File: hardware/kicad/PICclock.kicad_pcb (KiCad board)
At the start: 4 copper layers, 45 x 65 mm, 25 parts, among them J1 ICSP, J2 CLK_OUT, SW1 VAR/STEP, SW2 HS/[VAR/STEP], SW3 STEP, U1 PIC16F18344-P, U2 74HCT00, U3 EL7232CNZ, Y1 25MHz, Y2 CXO_DIP14

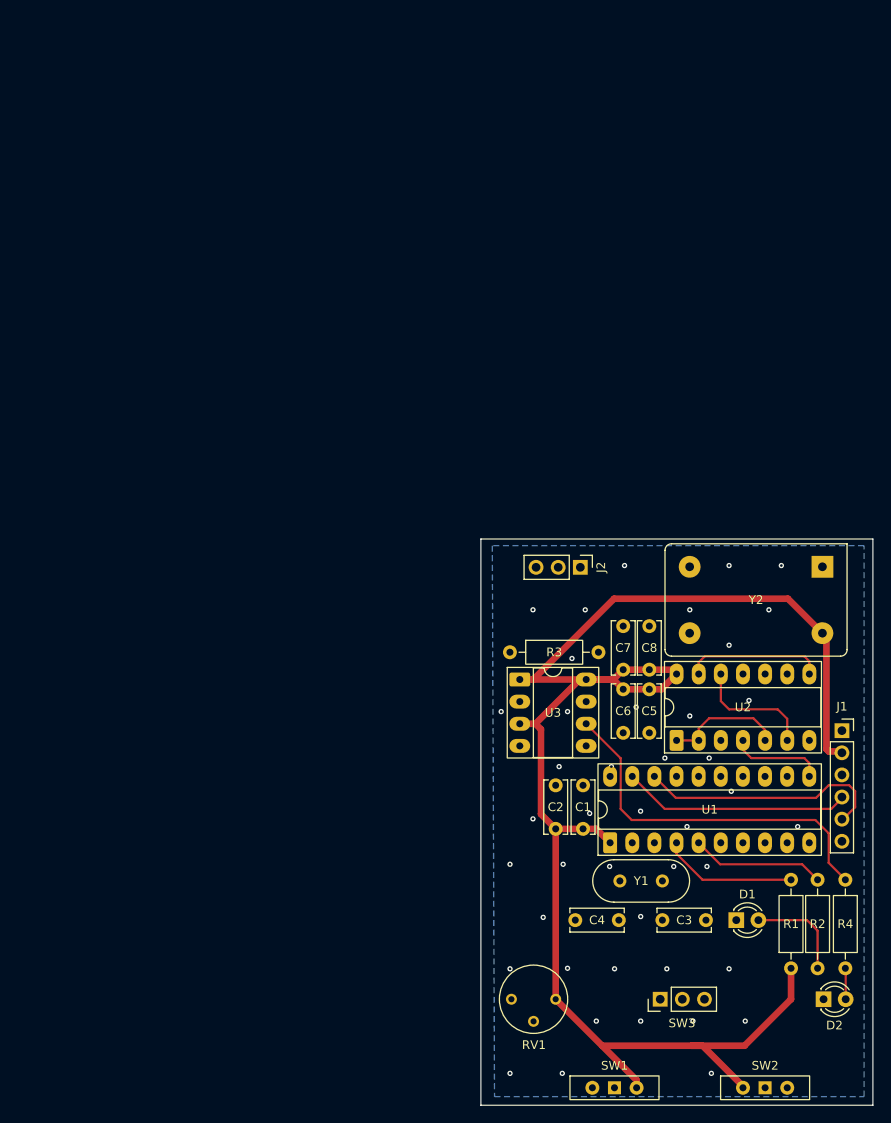
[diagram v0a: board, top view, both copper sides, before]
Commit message: add power input
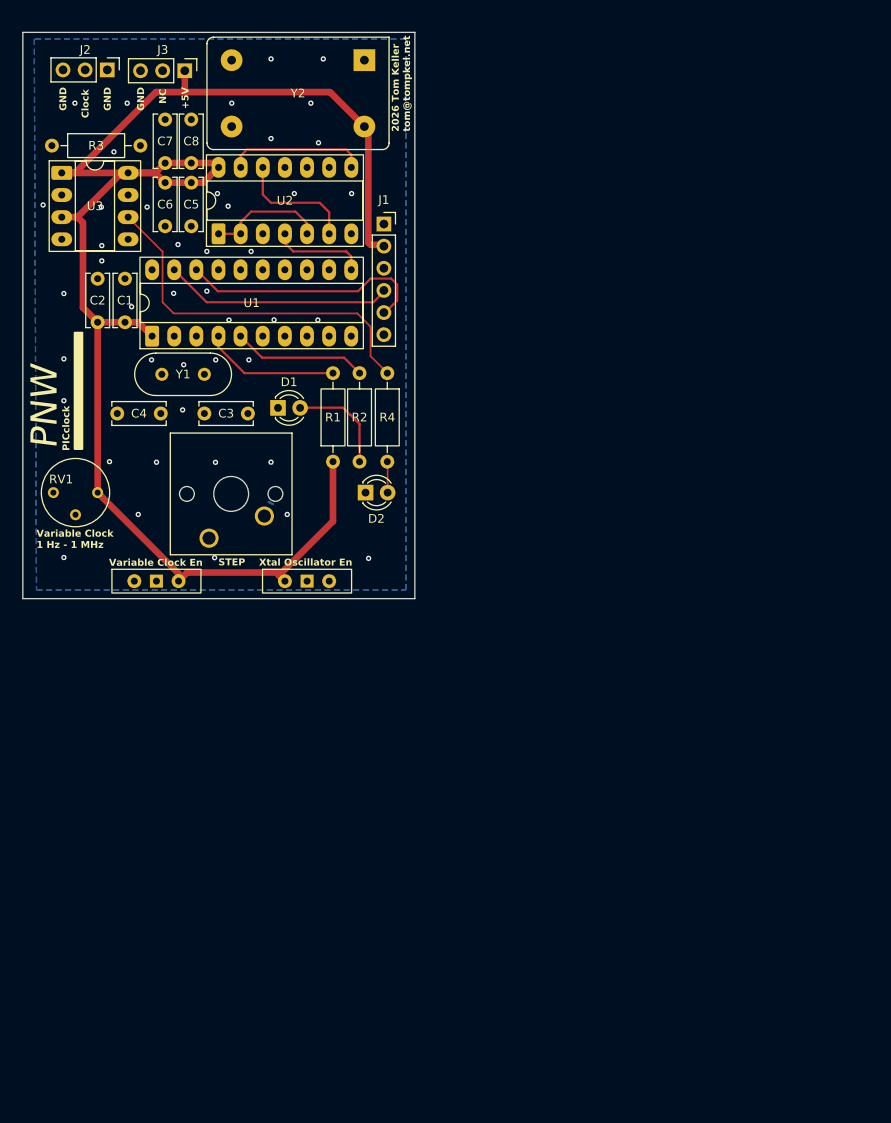
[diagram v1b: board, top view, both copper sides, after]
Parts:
- added J3: PWR_IN, Connector_PinHeader_2.54mm:PinHeader_1x03_P2.54mm_Vertical, F.Cu at (26.7, 9.75)
- SW3: footprint Connector_PinHeader_2.54mm:PinHeader_1x03_P2.54mm_Vertical -> Button_Switch_Keyboard:SW_Cherry_MX_1.00u_PCB
- moved D1 78.9 mm to (37.4, 48.5)
- moved J2 78.8 mm to (17.8, 9.65)
- moved SW1 78.4 mm to (23.4, 68.3)
- moved SW2 78.4 mm to (40.7, 68.3)
- moved C1 78.4 mm to (19.8, 33.6)
- moved C2 78.4 mm to (16.7, 38.6)
- moved C3 78.4 mm to (33.9, 49.1)
- moved C4 78.4 mm to (23.9, 49.1)
- moved C5 78.4 mm to (27.4, 27.6)
- moved C6 78.4 mm to (24.4, 22.6)
- moved C7 78.4 mm to (24.4, 15.3)
- moved C8 78.4 mm to (27.4, 20.3)
- moved D2 78.4 mm to (47.4, 58.2)
- moved J1 78.4 mm to (49.5, 27.3)
- moved R1 78.4 mm to (43.7, 54.6)
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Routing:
- net Net-(U1-RC4): track 20.8 -> 26.2 mm
- net Net-(J2-Pin_2): track 14.0 -> 10.3 mm
- net +5V: track 184.8 -> 181.7 mm
- net Net-(U1-RA4): track 11.5 -> 10.3 mm
- net Net-(U1-RA5): track 11.5 -> 10.4 mm
- net ~{STEP_SEL}: track 39.3 -> 38.4 mm
- net Net-(U3-IN_A): track 41.9 -> 41.3 mm
- net GND: vias 43 -> 44
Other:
- board text added: "+5V"
- board text added: "2026 Tom Keller tom@tompkel.net"
- board text added: "Clock"
- board text added: "GND"
- board text added: "NC"
- board text added: "PICclock"
- board text added: "PNW"
- board text added: "STEP"
- board text added: "Variable Clock 1 Hz - 1 MHz"
- board text added: "Variable Clock En"
- board text added: "Xtal Oscillator En"
